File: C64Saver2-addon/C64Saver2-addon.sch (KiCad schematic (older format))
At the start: 29 parts, among them J1 Conn_01x12_Female, J2 Conn_01x07_Female, J3 OLED_128x32_Conn_01x04_Male, SW1 SW_Push, SW2 SW_Push, U1 INA219xIDR-SOIC, U2 ISO1541D, U3 ProMicro, U4 PC817, U6 ACS712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

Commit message: ssop. 0603 capacitors
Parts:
- removed U4, U8: PC817, sop:SOP4-WIDE, symbol PC817
- added U4, U5: TLP291, Housings_SOIC:SO-4_7.6x3.6mm_Pitch2.54mm, symbol TLP291
- C3, C5: footprint Capacitors_SMD:C_0805_HandSoldering -> Capacitors_SMD:C_0603_HandSoldering
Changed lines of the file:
@@
 F 0 "C5" H 10575 4400 50  0000 L CNN
 F 1 "1u" H 10575 4200 50  0000 L CNN
-F 2 "Capacitors_SMD:C_0805_HandSoldering" H 10588 4150 50  0001 C CNN
+F 2 "Capacitors_SMD:C_0603_HandSoldering" H 10588 4150 50  0001 C CNN
 F 3 "" H 10550 4300 50  0001 C CNN
 	1    10550 4300
@@
 F 0 "C3" H 8425 1400 50  0000 L CNN
 F 1 "1u" H 8425 1200 50  0000 L CNN
-F 2 "Capacitors_SMD:C_0805_HandSoldering" H 8438 1150 50  0001 C CNN
+F 2 "Capacitors_SMD:C_0603_HandSoldering" H 8438 1150 50  0001 C CNN
 F 3 "" H 8400 1300 50  0001 C CNN
 	1    8400 1300
@@
 	1    0    0    -1
 $EndComp
-$Comp
-L PC817 U8
-U 1 1 5B3C18C9
+Wire Wire Line
+	4500 5050 4550 5050
+$Comp
+L TLP291 U4
+U 1 1 5B3D5BA2
 P 4850 5150
-F 0 "U8" H 4650 5350 50  0000 L CNN
-F 1 "PC817" H 4850 5350 50  0000 L CNN
-F 2 "sop:SOP4-WIDE" H 4650 4950 50  0001 L CIN
+F 0 "U4" H 4650 5350 50  0000 L CNN
+F 1 "TLP291" H 4850 5350 50  0000 L CNN
+F 2 "Housings_SOIC:SO-4_7.6x3.6mm_Pitch2.54mm" H 4650 4950 50  0001 L CIN
 F 3 "" H 4850 5150 50  0001 L CNN
 	1    4850 5150
@@
 $EndComp
 $Comp
-L PC817 U4
-U 1 1 5B3C21F6
+L TLP291 U5
+U 1 1 5B3D5E18
 P 4850 5900
-F 0 "U4" H 4650 6100 50  0000 L CNN
-F 1 "PC817" H 4850 6100 50  0000 L CNN
-F 2 "sop:SOP4-WIDE" H 4650 5700 50  0001 L CIN
+F 0 "U5" H 4650 6100 50  0000 L CNN
+F 1 "TLP291" H 4850 6100 50  0000 L CNN
+F 2 "Housings_SOIC:SO-4_7.6x3.6mm_Pitch2.54mm" H 4650 5700 50  0001 L CIN
 F 3 "" H 4850 5900 50  0001 L CNN
 	1    4850 5900
 	1    0    0    -1
 $EndComp
-Wire Wire Line
-	4500 5050 4550 5050
 $EndSCHEMATC

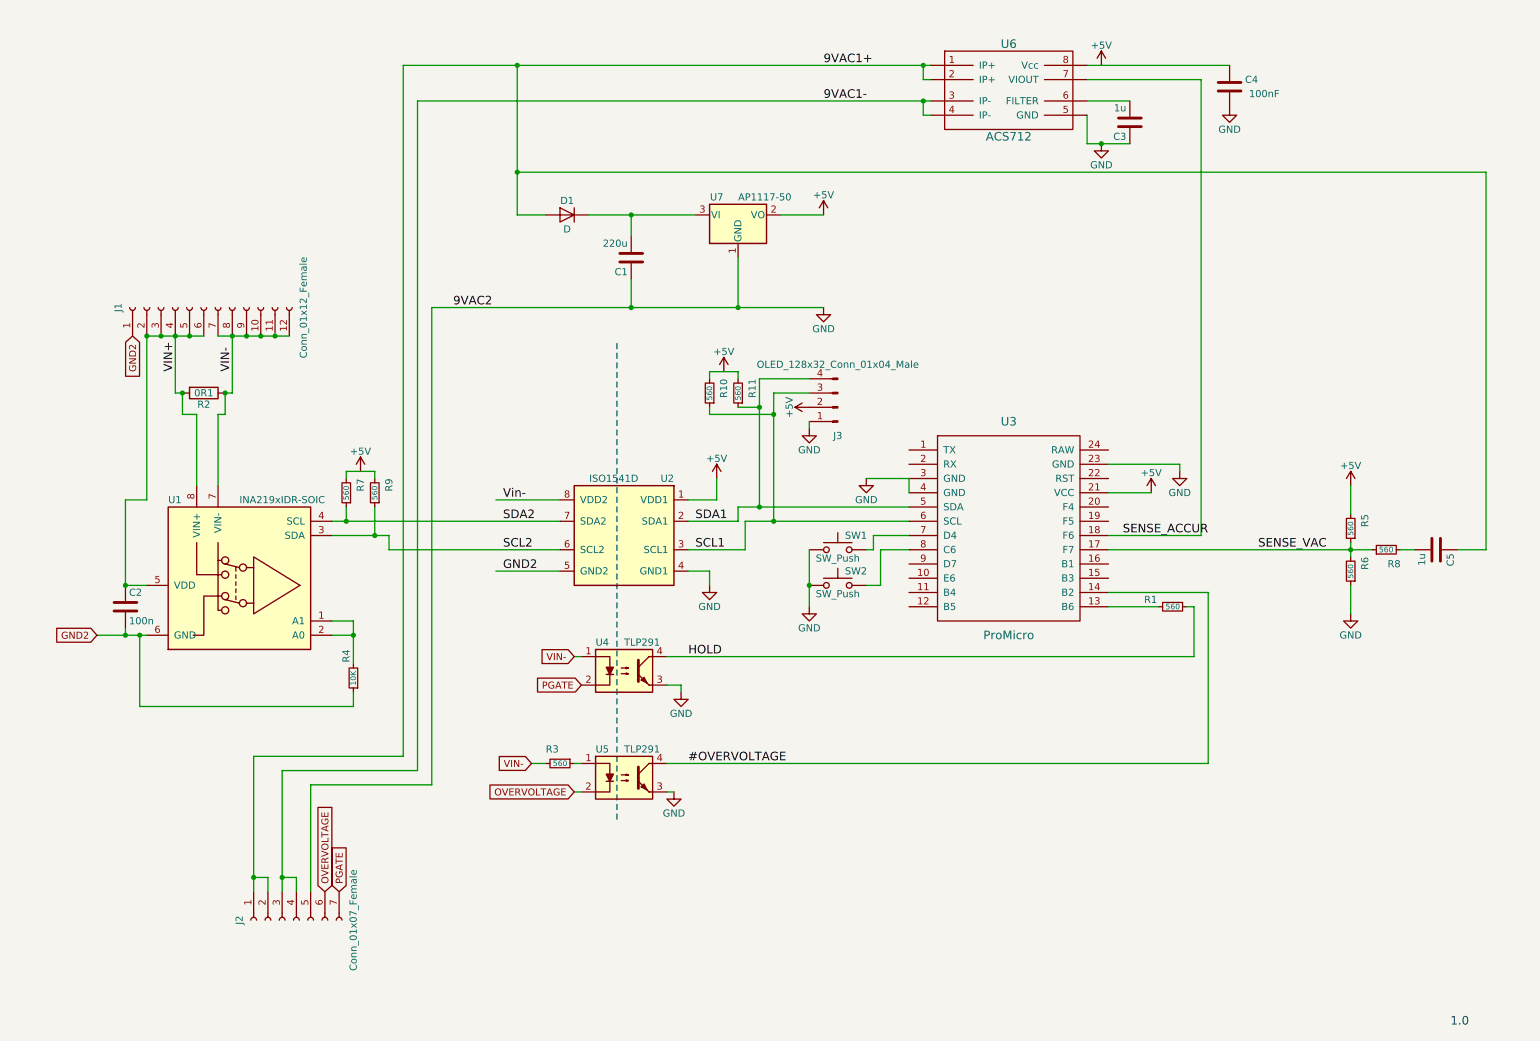
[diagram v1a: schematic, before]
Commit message: another regulator on 5v to protect the ina219 and iso1541
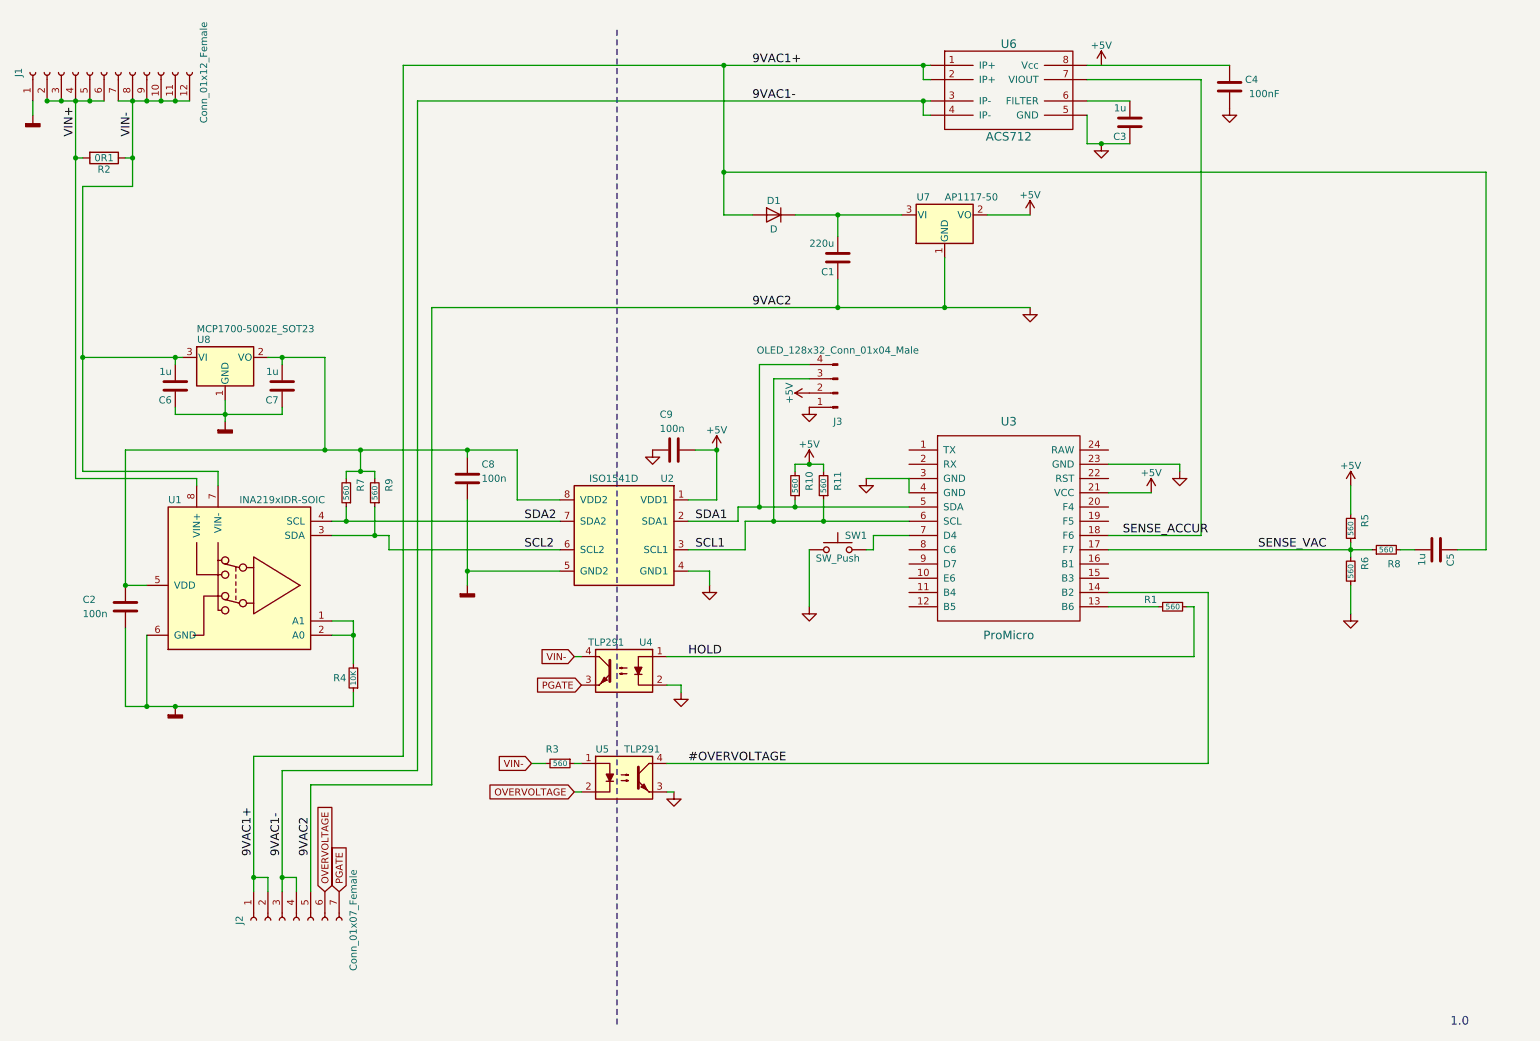
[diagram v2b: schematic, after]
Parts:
- removed SW2: SW_Push, Buttons_Switches_THT:SW_PUSH_6mm_h13mm, symbol SW_Push
- added C6, C7: 1u, Capacitors_SMD:C_0603_HandSoldering, symbol C
- added C8, C9: 100n, Capacitors_SMD:C_0603_HandSoldering, symbol C
- added U8: MCP1700-5002E_SOT23, TO_SOT_Packages_SMD:SOT-23, symbol MCP1700-5002E_SOT23
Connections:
- net Vin- is gone; now on an unnamed net: U2.8 (VDD2)
- net +5V: now also R10.2, R11.2, C9.1
- net GND: now also U4.2, C9.2; no longer U4.3
- net HOLD: now also U4.1; no longer U4.4
- net PGATE: now also U4.3; no longer U4.2
- net SCL1: now also R11.1; no longer R10.1
- net SDA1: now also R10.1; no longer R11.1
- net VIN+: no longer C2.1, U1.5 (VDD)
- net VIN-: now also U4.4, C6.2, U8.3 (VI); no longer U4.1
- net at R7.2, R9.2: now also C2.1, U1.5 (VDD), C7.2, C8.1, U8.2 (VO)
- net GND2 renamed GNDD
- net GNDD: now also C6.1, C7.1, C8.2, U8.1 (GND)
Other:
- moved on the sheet: C1, D1, J1, J3, R10, R11, R2, U7

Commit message: fit to hammond1591, larger board.
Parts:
- removed J2: Conn_01x07_Female, Pin_Headers:Pin_Header_Straight_1x07_Pitch2.54mm, symbol Conn_01x07_Female
- removed U7: AP1117-50, TO_SOT_Packages_SMD:SOT-223-3_TabPin2, symbol AP1117-50
- added C10: 1u, Capacitors_SMD:C_0603_HandSoldering, symbol C
- added J2: Conn_01x12_Female, Pin_Headers:Pin_Header_Straight_1x12_Pitch2.54mm, symbol Conn_01x12_Female
- added U7: MCP1700-5002E_SOT23, TO_SOT_Packages_SMD:SOT-23, symbol MCP1700-5002E_SOT23
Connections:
- net +5V: now also C10.2, U7.2 (VO)
- net 9VAC1+: now also J2.1 (Pin_1), J2.2 (Pin_2)
- net 9VAC1-: now also J2.3 (Pin_3), J2.4 (Pin_4)
- net GND: now also C10.1, J2.5 (Pin_5), U7.1 (GND)
- net OVERVOLTAGE: now also J2.6 (Pin_6)
- net PGATE: now also J2.7 (Pin_7)
- net at C1.2, D1.1 (K): now also U7.3 (VI)
- net VDD2: now reaches C2.1, C7.2, C8.1, R7.2, R9.2, U1.5 (VDD), U2.8 (VDD2), U8.2 (VO)

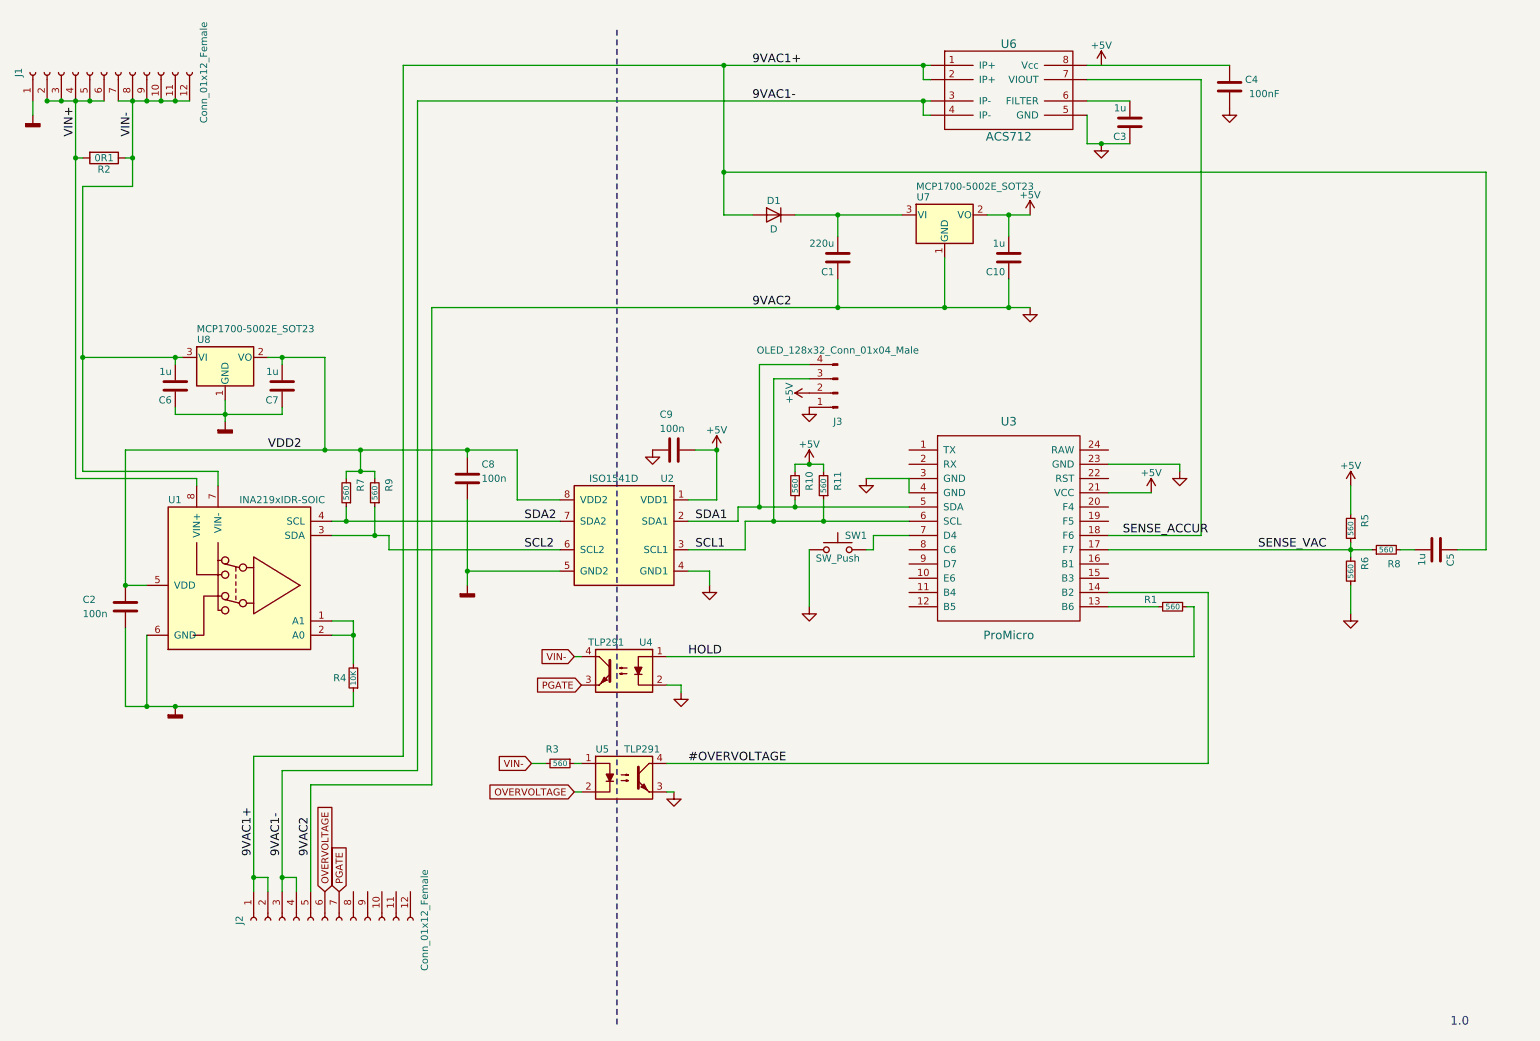
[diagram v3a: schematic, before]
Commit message: hammond1551G. It will be a tight fit !
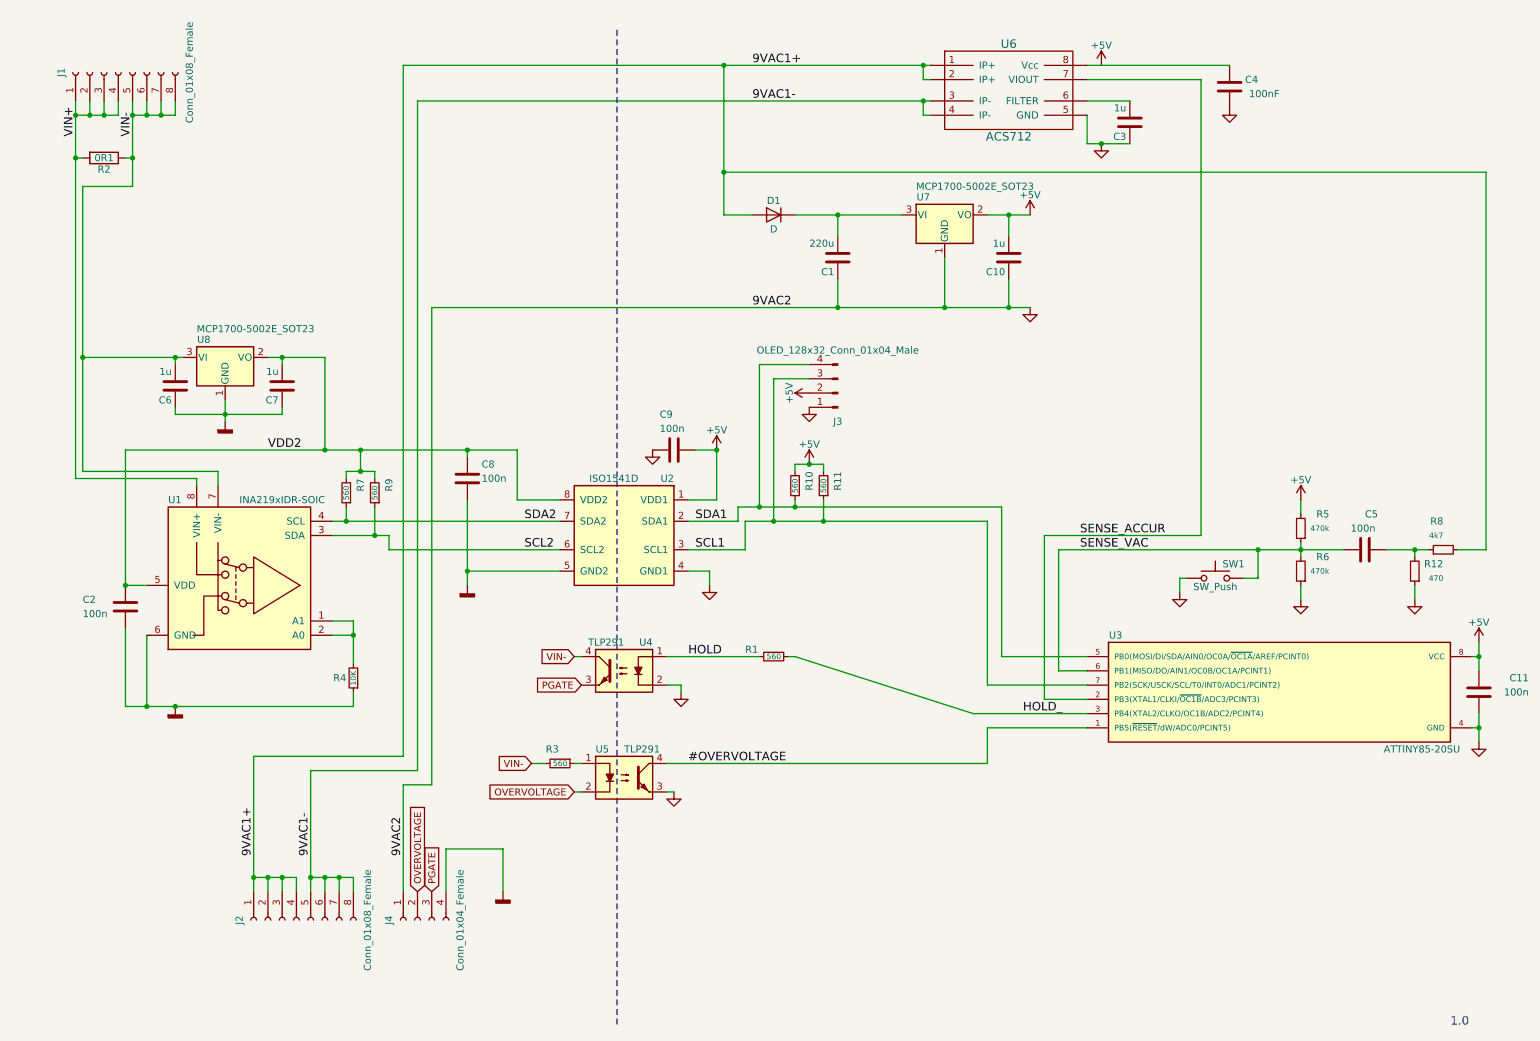
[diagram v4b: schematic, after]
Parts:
- removed J1, J2: Conn_01x12_Female, Pin_Headers:Pin_Header_Straight_1x12_Pitch2.54mm, symbol Conn_01x12_Female
- removed U3: ProMicro, promicro:ProMicro, symbol ProMicro
- added C11: 100n, Capacitors_SMD:C_0603_HandSoldering, symbol C
- added J1, J2: Conn_01x08_Female, Pin_Headers:Pin_Header_Straight_1x08_Pitch2.54mm, symbol Conn_01x08_Female
- added J4: Conn_01x04_Female, Pin_Headers:Pin_Header_Straight_1x04_Pitch2.54mm, symbol Conn_01x04_Female
- added R12: 470, Resistors_SMD:R_0603_HandSoldering, symbol R_Small
- added U3: ATTINY85-20SU, Housings_SOIC:SOIC-8_3.9x4.9mm_Pitch1.27mm, symbol ATTINY85-20SU
- C5: value 1u -> 100n
- R5, R6: value 560 -> 470k
- R8: value 560 -> 4k7
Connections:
- net #OVERVOLTAGE: now also U3.1 (PB5(~RESET~/dW/ADC0/PCINT5))
- net +5V: now also C11.2, U3.8 (VCC)
- net 9VAC1+: now also R8.2, J2.1 (Pin_1), J2.2 (Pin_2), J2.3 (Pin_3), J2.4 (Pin_4); no longer C5.1
- net 9VAC1-: now also J2.5 (Pin_5), J2.6 (Pin_6), J2.7 (Pin_7), J2.8 (Pin_8)
- net GND: now also C11.1, J4.1 (Pin_1), R12.1, U3.4 (GND)
- net GNDD: now also J4.4 (Pin_4)
- net HOLD: now also R1.2; no longer R1.1
- net OVERVOLTAGE: now also J4.2 (Pin_2)
- net PGATE: now also J4.3 (Pin_3)
- net SCL1: now also U3.7 (PB2(SCK/USCK/SCL/T0/INT0/ADC1/PCINT2))
- net SDA1: now also U3.5 (PB0(MOSI/DI/SDA/AIN0/OC0A/~OC1A~/AREF/PCINT0))
- net SENSE_ACCUR: now also U3.2 (PB3(XTAL1/CLKI/~OC1B~/ADC3/PCINT3))
- net SENSE_VAC: now also C5.2, SW1.2, U3.6 (PB1(MISO/DO/AIN1/OC0B/OC1A/PCINT1)); no longer R8.1
- net VIN+: now also J1.1 (Pin_1), J1.2 (Pin_2), J1.3 (Pin_3), J1.4 (Pin_4)
- net VIN-: now also J1.5 (Pin_5), J1.6 (Pin_6), J1.7 (Pin_7), J1.8 (Pin_8)
- new net: C5.1, R12.2, R8.1
- new net HOLD_: R1.1, U3.3 (PB4(XTAL2/CLKO/OC1B/ADC2/PCINT4))
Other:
- moved on the sheet: C5, R1, R5, R6, R8, SW1
